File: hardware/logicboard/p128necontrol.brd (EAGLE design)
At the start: 95 x 72 mm, 57 parts, among them IC1 74LS158N, IC10 74LS595D, IC11 74LS595D, IC12 74LS595D, IC13 74LS595D, IC14 74LS595D, IC15 74LS595D, IC16 74LS595D, IC17 74LS595D, IC2 74LS595D, IC3 74LS595D, IC4 74LS595D, IC5 74LS595D, IC6 74LS595D, IC7 74LS595D, IC8 74LS595D, IC9 74LS595D, J2 DIN5

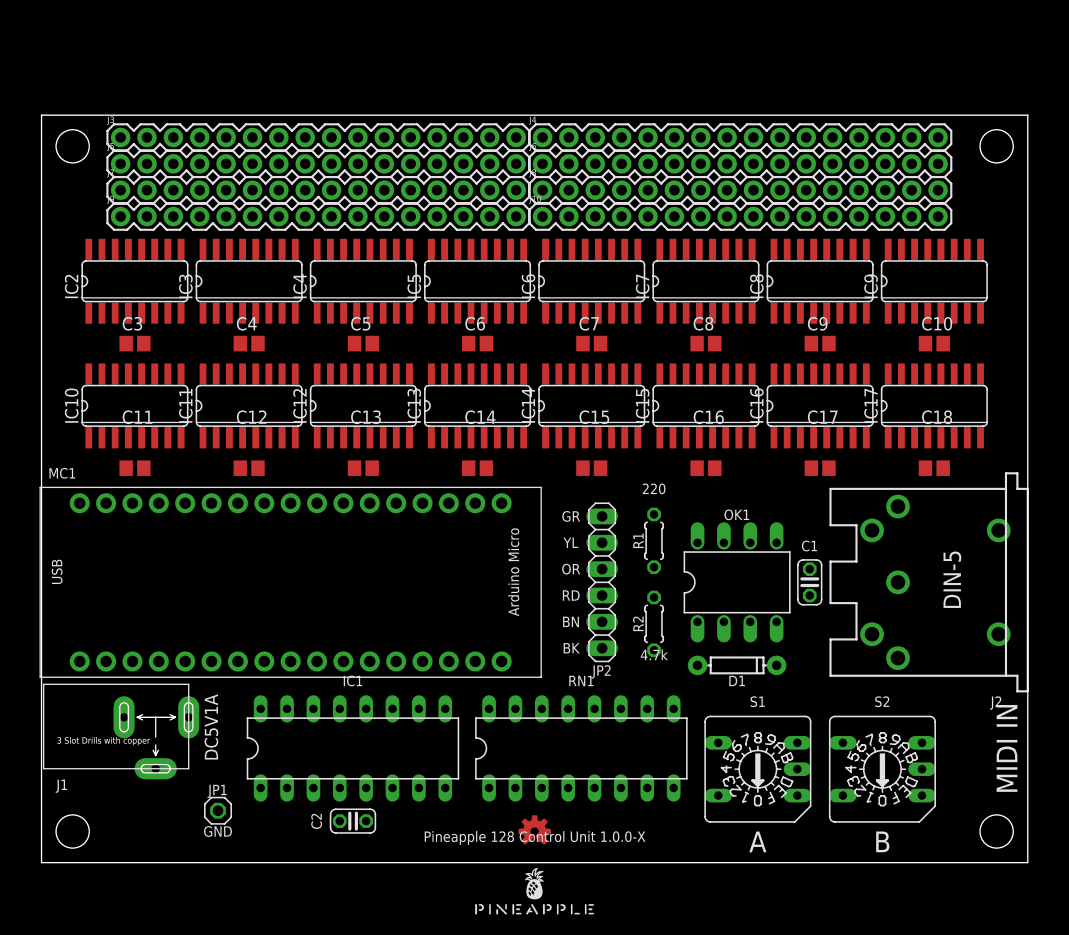
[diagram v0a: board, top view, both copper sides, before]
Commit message: Nocontrol 128-ch out.
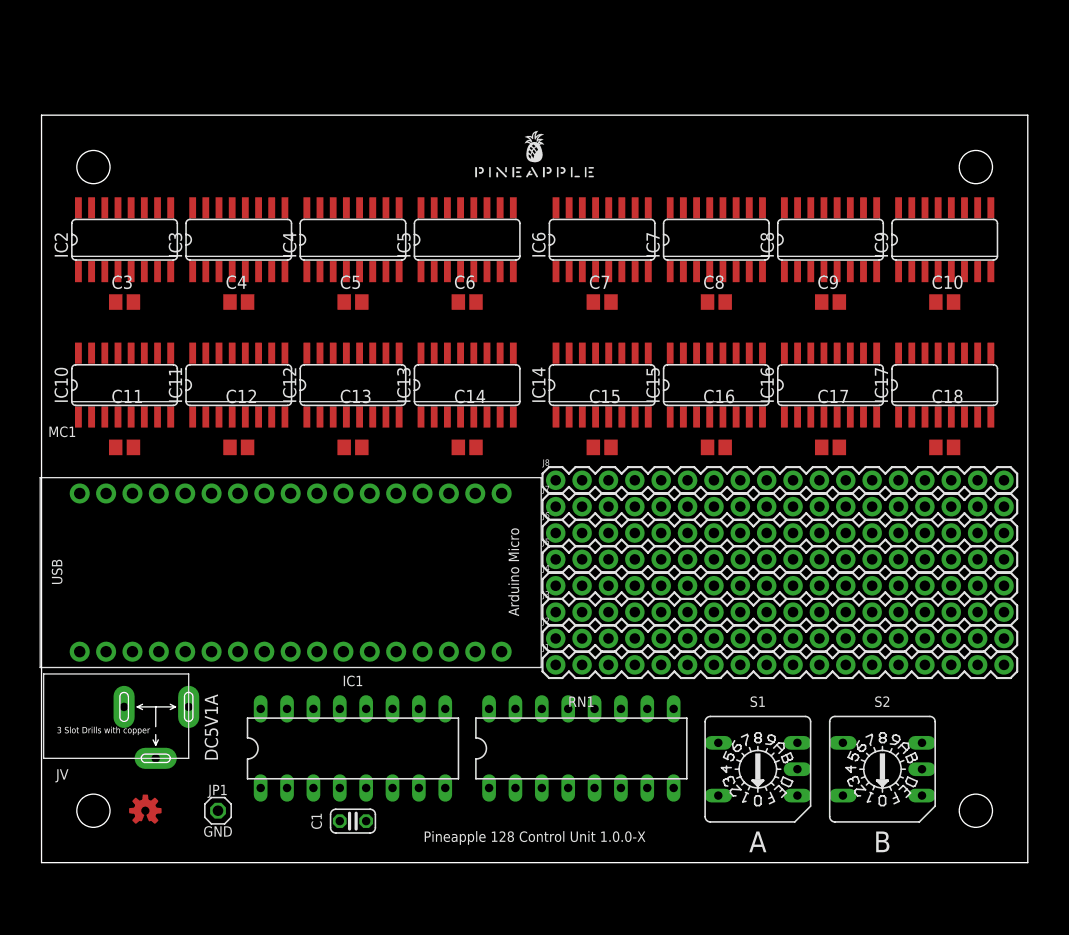
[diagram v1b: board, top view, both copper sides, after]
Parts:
- removed C2: (no value), resistor:C025-024X044
- removed D1: 200mA/100V/1V, SparkFun-DiscreteSemi:DIODE-1N4148
- removed J10, J9: (no value), SparkFun-Connectors:1X16
- removed JP2: (no value), pinhead:1X06
- removed OK1: 6N137, optocoupler:DIL08
- removed R1: 220, resistor:0204/5
- removed R2: 10k, resistor:0204/5
- added JV: (no value), Seeed-Connector:3P-L14.2*W11.0*H9.0MM
- J1: device Seeed-Connector:3P-L14.2*W11.0*H9.0MM -> SparkFun-Connectors:1X18
- J2: value DIN5 -> (none); device SparkFun-Connectors:DIN5-RA-PTH -> SparkFun-Connectors:1X18
- J3, J4, J5, J6, J7, J8: device SparkFun-Connectors:1X16 -> SparkFun-Connectors:1X18
- moved U$1 71.0 mm to (47.5, 66.0)
- moved J3 62.0 mm to (49.5, 24.1)
- moved J5 56.6 mm to (49.5, 29.2)
- moved J7 51.8 mm to (49.5, 34.3)
- moved C1 49.6 mm to (30.0, 4.00), turned to 180 degrees
- moved J2 45.8 mm to (49.5, 21.6), turned to 0 degrees
- moved J4 43.2 mm to (49.5, 26.7)
- moved J1 38.9 mm to (49.5, 19.1)
- moved LOGO1 37.6 mm to (10.0, 5.00)
- moved J6 35.6 mm to (49.5, 31.8)
- moved J8 28.0 mm to (49.5, 36.8)
- moved C10 4.12 mm to (87.0, 54.0)
- moved C3 4.12 mm to (8.00, 54.0)
- moved C4 4.12 mm to (19.0, 54.0)
- moved C5 4.12 mm to (30.0, 54.0)
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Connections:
- removed net MIRETN: D1.A, J2.5, OK1.3
- removed net MISEND: J2.4, R1.2
- removed net N$1: D1.C, OK1.2, R1.1
- net GND: now also J1.18, J1.9, J2.18, J2.9, J3.18, J3.9, J4.18, J4.9, J5.18, J5.9, J6.18, J6.9, J7.18, J7.9, J8.18, J8.9, JV.-1, JV.-2; no longer C2.2, J1.-1, J1.-2, JP2.1, JP2.2, OK1.5
- net N101: now also J1.1; no longer J3.1
- net N102: now also J1.2; no longer J3.2
- net N103: now also J1.3; no longer J3.3
- net N104: now also J1.4; no longer J3.4
- net N105: now also J1.5; no longer J3.5
- net N106: now also J1.6; no longer J3.6
- net N107: now also J1.7; no longer J3.7
- net N108: now also J1.8; no longer J3.8
- net N109: now also J1.10; no longer J3.9
- net N110: now also J1.11; no longer J3.10
- net N111: now also J1.12; no longer J3.11
- net N112: now also J1.13; no longer J3.12
- net N113: now also J1.14; no longer J3.13
- net N114: now also J1.15; no longer J3.14
- net N115: now also J1.16; no longer J3.15
- net N116: now also J1.17; no longer J3.16
- net N201: now also J2.1; no longer J4.1
- net N202: now also J2.2; no longer J4.2
- net N203: now also J2.3; no longer J4.3
- net N204: now also J2.4; no longer J4.4
- net N205: now also J2.5; no longer J4.5
- net N206: now also J2.6; no longer J4.6
- net N207: now also J2.7; no longer J4.7
- net N208: now also J2.8; no longer J4.8
- net N209: now also J2.10; no longer J4.9
- net N210: now also J2.11; no longer J4.10
- net N211: now also J2.12; no longer J4.11
- net N212: now also J2.13; no longer J4.12
- net N213: now also J2.14; no longer J4.13
- net N214: now also J2.15; no longer J4.14
- net N215: now also J2.16; no longer J4.15
- net N216: now also J2.17; no longer J4.16
- net N301: now also J3.1; no longer J5.1
- net N302: now also J3.2; no longer J5.2
- net N303: now also J3.3; no longer J5.3
- net N304: now also J3.4; no longer J5.4
- net N305: now also J3.5; no longer J5.5
- net N306: now also J3.6; no longer J5.6
- net N307: now also J3.7; no longer J5.7
- net N308: now also J3.8; no longer J5.8
- net N309: now also J3.10; no longer J5.9
- net N310: now also J3.11; no longer J5.10
- net N311: now also J3.12; no longer J5.11
- net N312: now also J3.13; no longer J5.12
- net N313: now also J3.14; no longer J5.13
- net N314: now also J3.15; no longer J5.14
- net N315: now also J3.16; no longer J5.15
- net N316: now also J3.17; no longer J5.16
- net N401: now also J4.1; no longer J6.1
- net N402: now also J4.2; no longer J6.2
- net N403: now also J4.3; no longer J6.3
- net N404: now also J4.4; no longer J6.4
- net N405: now also J4.5; no longer J6.5
- net N406: now also J4.6; no longer J6.6
- net N407: now also J4.7; no longer J6.7
- net N408: now also J4.8; no longer J6.8
- net N409: now also J4.10; no longer J6.9
- net N410: now also J4.11; no longer J6.10
- net N411: now also J4.12; no longer J6.11
- net N412: now also J4.13; no longer J6.12
- net N413: now also J4.14; no longer J6.13
- net N414: now also J4.15; no longer J6.14
- net N415: now also J4.16; no longer J6.15
- net N416: now also J4.17; no longer J6.16
- net N501: now also J5.1; no longer J7.1
- net N502: now also J5.2; no longer J7.2
- net N503: now also J5.3; no longer J7.3
- net N504: now also J5.4; no longer J7.4
- net N505: now also J5.5; no longer J7.5
- net N506: now also J5.6; no longer J7.6
- net N507: now also J5.7; no longer J7.7
- net N508: now also J5.8; no longer J7.8
- net N509: now also J5.10; no longer J7.9
- net N510: now also J5.11; no longer J7.10
- net N511: now also J5.12; no longer J7.11
- net N512: now also J5.13; no longer J7.12
- net N513: now also J5.14; no longer J7.13
- net N514: now also J5.15; no longer J7.14
- net N515: now also J5.16; no longer J7.15
- net N516: now also J5.17; no longer J7.16
- net N601: now also J6.1; no longer J8.1
- net N602: now also J6.2; no longer J8.2
- net N603: now also J6.3; no longer J8.3
- net N604: now also J6.4; no longer J8.4
- net N605: now also J6.5; no longer J8.5
- net N606: now also J6.6; no longer J8.6
- net N607: now also J6.7; no longer J8.7
- net N608: now also J6.8; no longer J8.8
- net N609: now also J6.10; no longer J8.9
- net N610: now also J6.11; no longer J8.10
- net N611: now also J6.12; no longer J8.11
- net N612: now also J6.13; no longer J8.12
- net N613: now also J6.14; no longer J8.13
- net N614: now also J6.15; no longer J8.14
- net N615: now also J6.16; no longer J8.15
- net N616: now also J6.17; no longer J8.16
- net N701: now also J7.1; no longer J9.1
- net N702: now also J7.2; no longer J9.2
- net N703: now also J7.3; no longer J9.3
- net N704: now also J7.4; no longer J9.4
- net N705: now also J7.5; no longer J9.5
- net N706: now also J7.6; no longer J9.6
- net N707: now also J7.7; no longer J9.7
- net N708: now also J7.8; no longer J9.8
- net N709: now also J7.10; no longer J9.9
- net N710: now also J7.11; no longer J9.10
- net N711: now also J7.12; no longer J9.11
- net N712: now also J7.13; no longer J9.12
- net N713: now also J7.14; no longer J9.13
- net N714: now also J7.15; no longer J9.14
- net N715: now also J7.16; no longer J9.15
- net N716: now also J7.17; no longer J9.16
- net N801: now also J8.1; no longer J10.1
- net N802: now also J8.2; no longer J10.2
- net N803: now also J8.3; no longer J10.3
- net N804: now also J8.4; no longer J10.4
- net N805: now also J8.5; no longer J10.5
- net N806: now also J8.6; no longer J10.6
- net N807: now also J8.7; no longer J10.7
- net N808: now also J8.8; no longer J10.8
- net N809: now also J8.10; no longer J10.9
- net N810: now also J8.11; no longer J10.10
- net N811: now also J8.12; no longer J10.11
- net N812: now also J8.13; no longer J10.12
- net N813: now also J8.14; no longer J10.13
- net N814: now also J8.15; no longer J10.14
- net N815: now also J8.16; no longer J10.15
- net N816: now also J8.17; no longer J10.16
- net RX: no longer JP2.4, OK1.6, R2.1
- net TX: no longer JP2.5
- net VCC: now also JV.+; no longer C2.1, J1.+, JP2.3, OK1.7, OK1.8, R2.2
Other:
- board text removed: "220"
- board text removed: "4.7k"
- board text removed: "BK"
- board text removed: "BN"
- board text removed: "GR"
- board text removed: "MIDI IN"
- board text removed: "OR"
- board text removed: "RD"
- board text removed: "YL"

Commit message: First working necontrol.
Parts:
- removed C10, C11, C12, C13, C14, C15, C16, C17, C18, C9: (no value), resistor:C2012
- removed IC10, IC11, IC12, IC13, IC14, IC15, IC16, IC17, IC9: 74LS595D, 74xx-us:SO16
- removed RN1: 10k, resistor-dil:DIL16
- removed S1, S2: (no value), switch-dil:A1353HEX
- added C2: (no value), resistor:C025-024X044
- added SV1, SV2, SV3: (no value), con-ml:ML14
- C3, C4, C5, C6, C7, C8: device resistor:C2012 -> resistor:C025-024X044
- IC1: value 74LS158N -> 74LS595N
- IC2, IC3, IC4, IC5, IC6, IC7, IC8: value 74LS595D -> 74LS595N; device 74xx-us:SO16 -> 74xx-us:DIL16
- J1, J2, J3, J4, J5, J6, J7, J8: device SparkFun-Connectors:1X18 -> SparkFun-Connectors:1X10
- moved C1 61.1 mm to (8.00, 61.0)
- moved IC1 43.9 mm to (8.00, 49.0), turned to 270 degrees
- moved J1 29.6 mm to (24.1, 3.81)
- moved J2 29.6 mm to (24.1, 6.35)
- moved J3 28.4 mm to (24.1, 11.4)
- moved J4 28.4 mm to (24.1, 14.0)
- moved J5 25.5 mm to (52.1, 3.81)
- moved J6 25.5 mm to (52.1, 6.35)
- moved C5 25.0 mm to (54.0, 61.0)
- moved C6 25.0 mm to (65.0, 61.0)
- moved C3 23.1 mm to (30.0, 61.0)
- moved C4 23.1 mm to (41.0, 61.0)
- moved C7 23.1 mm to (76.0, 61.0)
- moved C8 23.1 mm to (87.0, 61.0)
- moved J7 23.0 mm to (52.1, 11.4)
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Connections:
- removed net N$2: IC2.9, IC3.14
- removed net N$3: IC4.9, IC5.14
- removed net N$4: IC6.9, IC7.14
- removed net N$5: IC8.9, IC9.14
- removed net N$6: IC10.9, IC11.14
- removed net N$7: IC12.9, IC13.14
- removed net N$8: IC14.9, IC15.14
- removed net N$9: IC16.9, IC17.14
- removed net N109: IC3.15, J1.10
- removed net N110: IC3.1, J1.11
- removed net N111: IC3.2, J1.12
- removed net N112: IC3.3, J1.13
- removed net N113: IC3.4, J1.14
- removed net N114: IC3.5, J1.15
- removed net N115: IC3.6, J1.16
- removed net N116: IC3.7, J1.17
- removed net N209: IC5.15, J2.10
- removed net N210: IC5.1, J2.11
- removed net N211: IC5.2, J2.12
- removed net N212: IC5.3, J2.13
- removed net N213: IC5.4, J2.14
- removed net N214: IC5.5, J2.15
- removed net N215: IC5.6, J2.16
- removed net N216: IC5.7, J2.17
- removed net N309: IC7.15, J3.10
- removed net N310: IC7.1, J3.11
- removed net N311: IC7.2, J3.12
- removed net N312: IC7.3, J3.13
- removed net N313: IC7.4, J3.14
- removed net N314: IC7.5, J3.15
- removed net N315: IC7.6, J3.16
- removed net N316: IC7.7, J3.17
- removed net N409: IC9.15, J4.10
- removed net N410: IC9.1, J4.11
- removed net N411: IC9.2, J4.12
- removed net N412: IC9.3, J4.13
- removed net N413: IC9.4, J4.14
- removed net N414: IC9.5, J4.15
- removed net N415: IC9.6, J4.16
- removed net N416: IC9.7, J4.17
- removed net N509: IC11.15, J5.10
- removed net N510: IC11.1, J5.11
- removed net N511: IC11.2, J5.12
- removed net N512: IC11.3, J5.13
- removed net N513: IC11.4, J5.14
- removed net N514: IC11.5, J5.15
- removed net N515: IC11.6, J5.16
- removed net N516: IC11.7, J5.17
- removed net N609: IC13.15, J6.10
- removed net N610: IC13.1, J6.11
- removed net N611: IC13.2, J6.12
- removed net N612: IC13.3, J6.13
- removed net N613: IC13.4, J6.14
- removed net N614: IC13.5, J6.15
- removed net N615: IC13.6, J6.16
- removed net N616: IC13.7, J6.17
- removed net N709: IC15.15, J7.10
- removed net N710: IC15.1, J7.11
- removed net N711: IC15.2, J7.12
- removed net N712: IC15.3, J7.13
- removed net N713: IC15.4, J7.14
- removed net N714: IC15.5, J7.15
- removed net N715: IC15.6, J7.16
- removed net N716: IC15.7, J7.17
- removed net N809: IC17.15, J8.10
- removed net N810: IC17.1, J8.11
- removed net N811: IC17.2, J8.12
- removed net N812: IC17.3, J8.13
- removed net N813: IC17.4, J8.14
- removed net N814: IC17.5, J8.15
- removed net N815: IC17.6, J8.16
- removed net N816: IC17.7, J8.17
- removed net SWA1: IC1.2, RN1.1, S1.1
- removed net SWA2: IC1.5, RN1.3, S1.4
- removed net SWA4: IC1.11, RN1.5, S1.8
- removed net SWA8: IC1.14, RN1.7, S1.2
- removed net SWB1: IC1.3, RN1.2, S2.1
- removed net SWB2: IC1.6, RN1.4, S2.4
- removed net SWB4: IC1.10, RN1.6, S2.8
- removed net SWB8: IC1.13, RN1.8, S2.2
- new net SIN1: IC1.14, SV2.6
- new net SIN2: IC2.14, SV2.7
- new net SIN3: IC3.14, SV2.8
- new net SIN4: IC4.14, SV2.9
- new net SIN5: IC5.14, SV2.10
- new net SIN6: IC6.14, SV2.11
- new net SIN7: IC7.14, SV2.12
- new net SIN8: IC8.14, SV2.13
- new net XOUT1: IC1.9, SV3.6
- new net XOUT2: IC2.9, SV3.7
- new net XOUT3: IC3.9, SV3.8
- new net XOUT4: IC4.9, SV3.9
- new net XOUT5: IC5.9, SV3.10
- new net XOUT6: IC6.9, SV3.11
- new net XOUT7: IC7.9, SV3.12
- new net XOUT8: IC8.9, SV3.13
- net CLR: now also IC1.10, SV1.3, SV2.3, SV3.3; no longer IC10.10, IC11.10, IC12.10, IC13.10, IC14.10, IC15.10, IC16.10, IC17.10, IC9.10
- net GND: now also C2.2, IC1.13, J1.10, J2.10, J3.10, J4.10, J5.10, J6.10, J7.10, J8.10, SV1.14, SV1.2, SV2.14, SV2.2, SV3.14, SV3.2; no longer C10.2, C11.2, C12.2, C13.2, C14.2, C15.2, C16.2, C17.2, C18.2, C9.2, IC1.15, IC10.13, IC10.8, IC11.13, IC11.8, IC12.13, IC12.8, IC13.13, IC13.8, IC14.13, IC14.8, IC15.13, IC15.8, IC16.13, IC16.8, IC17.13, IC17.8, IC9.13, IC9.8, J1.18, J2.18, J3.18, J4.18, J5.18, J6.18, J7.18, J8.18, S1.C, S2.C
- net N101: now also IC1.15; no longer IC2.15
- net N102: now also IC1.1; no longer IC2.1
- net N103: now also IC1.2; no longer IC2.2
- net N104: now also IC1.3; no longer IC2.3
- net N105: now also IC1.4; no longer IC2.4
- net N106: now also IC1.5; no longer IC2.5
- net N107: now also IC1.6; no longer IC2.6
- net N108: now also IC1.7; no longer IC2.7
- net N201: now also IC2.15; no longer IC4.15
- net N202: now also IC2.1; no longer IC4.1
- net N203: now also IC2.2; no longer IC4.2
- net N204: now also IC2.3; no longer IC4.3
- net N205: now also IC2.4; no longer IC4.4
- net N206: now also IC2.5; no longer IC4.5
- net N207: now also IC2.6; no longer IC4.6
- net N208: now also IC2.7; no longer IC4.7
- net N301: now also IC3.15; no longer IC6.15
- net N302: now also IC3.1; no longer IC6.1
- net N303: now also IC3.2; no longer IC6.2
- net N304: now also IC3.3; no longer IC6.3
- net N305: now also IC3.4; no longer IC6.4
- net N306: now also IC3.5; no longer IC6.5
- net N307: now also IC3.6; no longer IC6.6
- net N308: now also IC3.7; no longer IC6.7
- net N401: now also IC4.15; no longer IC8.15
- net N402: now also IC4.1; no longer IC8.1
- net N403: now also IC4.2; no longer IC8.2
- net N404: now also IC4.3; no longer IC8.3
- net N405: now also IC4.4; no longer IC8.4
- net N406: now also IC4.5; no longer IC8.5
- net N407: now also IC4.6; no longer IC8.6
- net N408: now also IC4.7; no longer IC8.7
- net N501: now also IC5.15; no longer IC10.15
- net N502: now also IC5.1; no longer IC10.1
- net N503: now also IC5.2; no longer IC10.2
- net N504: now also IC5.3; no longer IC10.3
- net N505: now also IC5.4; no longer IC10.4
- net N506: now also IC5.5; no longer IC10.5
- net N507: now also IC5.6; no longer IC10.6
- net N508: now also IC5.7; no longer IC10.7
- net N601: now also IC6.15; no longer IC12.15
- net N602: now also IC6.1; no longer IC12.1
- net N603: now also IC6.2; no longer IC12.2
- net N604: now also IC6.3; no longer IC12.3
- net N605: now also IC6.4; no longer IC12.4
- net N606: now also IC6.5; no longer IC12.5
- net N607: now also IC6.6; no longer IC12.6
- net N608: now also IC6.7; no longer IC12.7
- net N701: now also IC7.15; no longer IC14.15
- net N702: now also IC7.1; no longer IC14.1
- net N703: now also IC7.2; no longer IC14.2
- net N704: now also IC7.3; no longer IC14.3
- net N705: now also IC7.4; no longer IC14.4
- net N706: now also IC7.5; no longer IC14.5
- net N707: now also IC7.6; no longer IC14.6
- net N708: now also IC7.7; no longer IC14.7
- net N801: now also IC8.15; no longer IC16.15
- net N802: now also IC8.1; no longer IC16.1
- net N803: now also IC8.2; no longer IC16.2
- net N804: now also IC8.3; no longer IC16.3
- net N805: now also IC8.4; no longer IC16.4
- net N806: now also IC8.5; no longer IC16.5
- net N807: now also IC8.6; no longer IC16.6
- net N808: now also IC8.7; no longer IC16.7
- net RCLK: now also IC1.12, SV1.5, SV2.5, SV3.5; no longer IC10.12, IC11.12, IC12.12, IC13.12, IC14.12, IC15.12, IC16.12, IC17.12, IC9.12
- net SCLK: now also IC1.11, SV1.4, SV2.4, SV3.4; no longer IC10.11, IC11.11, IC12.11, IC13.11, IC14.11, IC15.11, IC16.11, IC17.11, IC9.11
- net SOUT1: now also SV1.6; no longer IC2.14
- net SOUT2: now also SV1.7; no longer IC4.14
- net SOUT3: now also SV1.8; no longer IC6.14
- net SOUT4: now also SV1.9; no longer IC8.14
- net SOUT5: now also SV1.10; no longer IC10.14
- net SOUT6: now also SV1.11; no longer IC12.14
- net SOUT7: now also SV1.12; no longer IC14.14
- net SOUT8: now also SV1.13; no longer IC16.14
- net SW1: no longer IC1.4
- net SW2: no longer IC1.7
- net SW4: no longer IC1.9
- net SW8: no longer IC1.12
- net SWSEL: no longer IC1.1
- net VCC: now also C2.1, SV1.1, SV2.1, SV3.1; no longer C10.1, C11.1, C12.1, C13.1, C14.1, C15.1, C16.1, C17.1, C18.1, C9.1, IC10.16, IC11.16, IC12.16, IC13.16, IC14.16, IC15.16, IC16.16, IC17.16, IC9.16, RN1.10, RN1.11, RN1.12, RN1.13, RN1.14, RN1.15, RN1.16, RN1.9
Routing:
- net GND: track 0.00 -> 571.8 mm, vias 0 -> 4
- net CLR: track 0.00 -> 255.5 mm, vias 0 -> 12
- net SCLK: track 0.00 -> 252.4 mm, vias 0 -> 7
- net VCC: track 0.00 -> 240.5 mm, vias 0 -> 2
- net RCLK: track 0.00 -> 235.3 mm, vias 0 -> 9
- net XOUT1: track 0.00 -> 104.1 mm, vias 0 -> 4
- net N802: track 0.00 -> 103.3 mm
- net N201: track 0.00 -> 93.4 mm, vias 0 -> 3
- net N702: track 0.00 -> 85.6 mm, vias 0 -> 2
- net N803: track 0.00 -> 85.4 mm, vias 0 -> 2
- net N804: track 0.00 -> 81.4 mm
- net N202: track 0.00 -> 79.9 mm, vias 0 -> 2
- net N106: track 0.00 -> 77.6 mm
- net N108: track 0.00 -> 77.1 mm
- net N105: track 0.00 -> 77.0 mm
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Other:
- board text removed: "A"
- board text removed: "B"

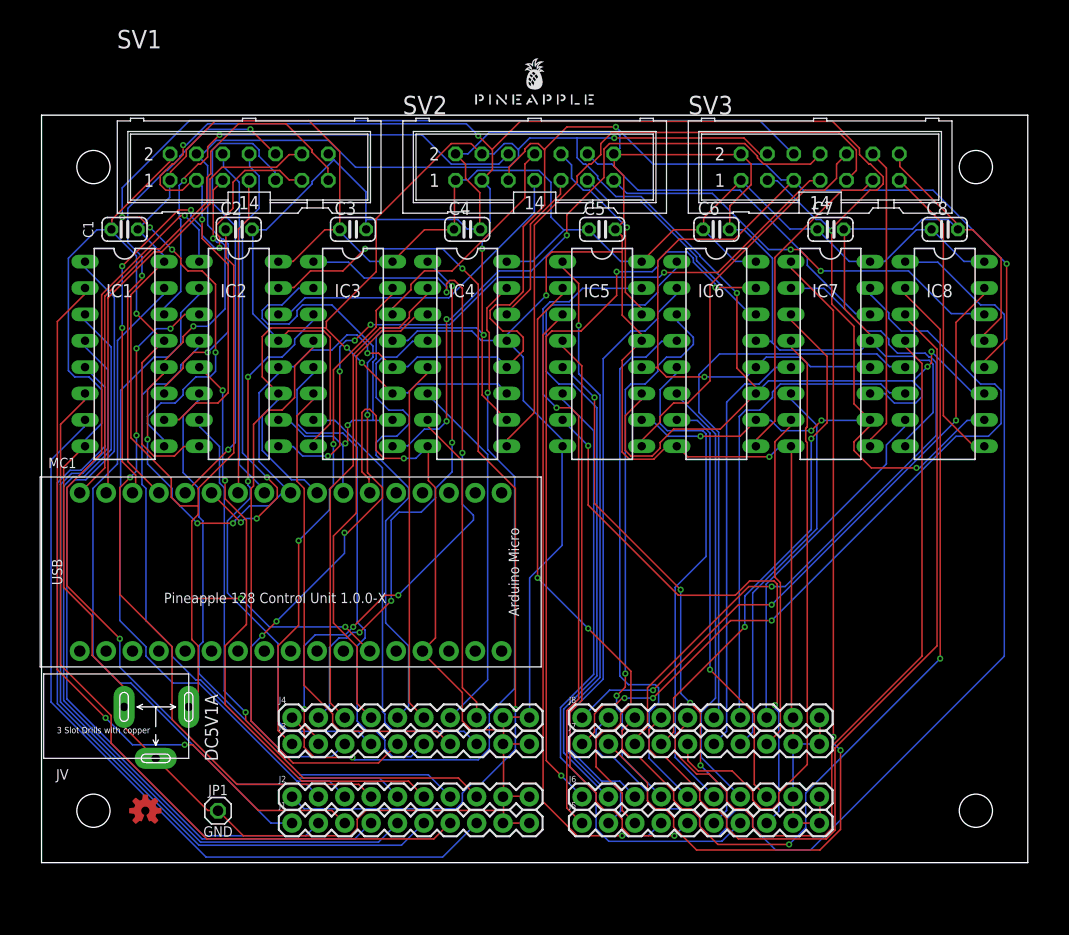
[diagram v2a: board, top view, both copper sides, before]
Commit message: Compiled Necontrol.
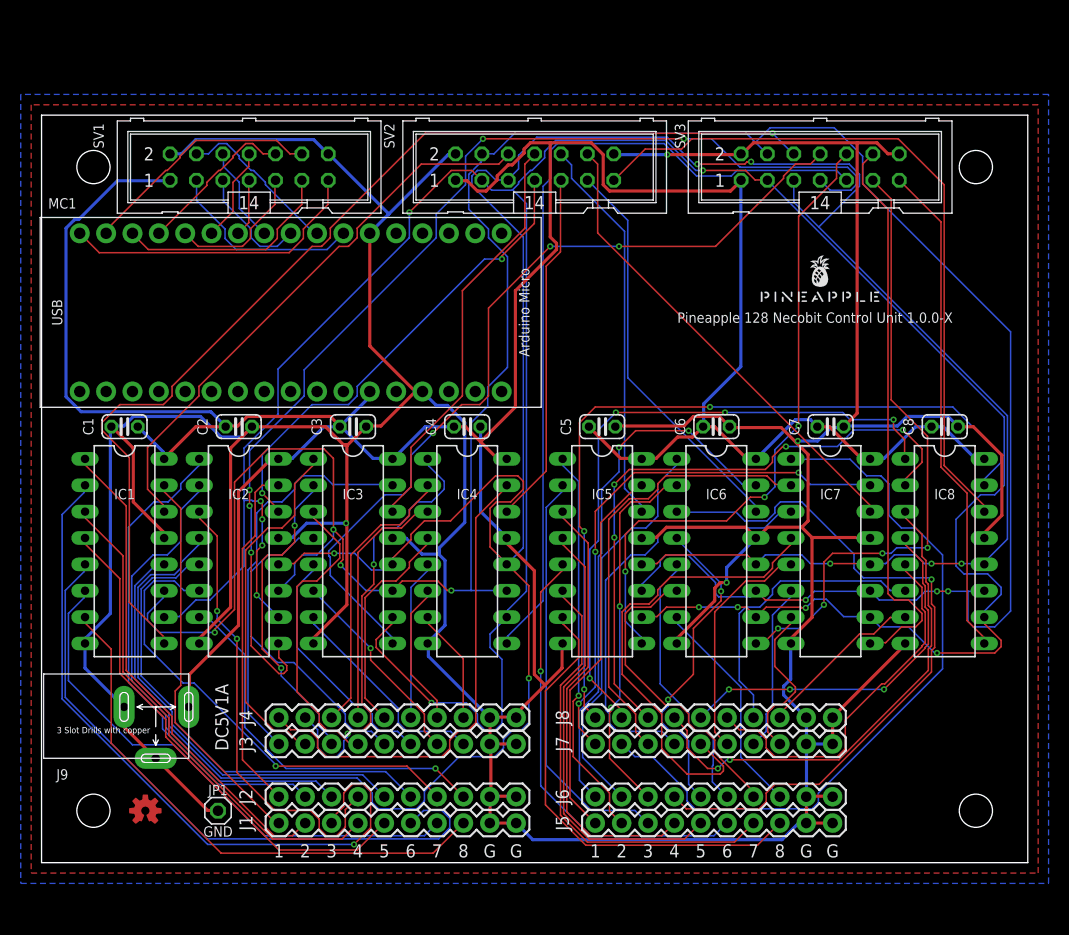
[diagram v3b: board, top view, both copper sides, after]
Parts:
- C1, C2, C3, C4, C5, C6, C7, C8: value (none) -> 0.01u
- SV1: value (none) -> OUT
- SV2: value (none) -> IN
- SV3: value (none) -> THRU
- moved U$1 33.4 mm to (75.0, 54.0)
- moved U$2 25.0 mm to (24.0, 53.0)
- moved C1 19.0 mm to (8.00, 42.0)
- moved C2 19.0 mm to (19.0, 42.0)
- moved C3 19.0 mm to (30.0, 42.0)
- moved C4 19.0 mm to (41.0, 42.0)
- moved C5 19.0 mm to (54.0, 42.0)
- moved C6 19.0 mm to (65.0, 42.0)
- moved C7 19.0 mm to (76.0, 42.0)
- moved C8 19.0 mm to (87.0, 42.0)
- moved IC1 19.0 mm to (8.00, 30.0)
- moved IC2 19.0 mm to (19.0, 30.0)
- moved IC3 19.0 mm to (30.0, 30.0)
- moved IC4 19.0 mm to (41.0, 30.0)
- moved IC5 19.0 mm to (54.0, 30.0)
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- renumbered JV to J9
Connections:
- removed net SW1: U$2.P$31
- removed net SW2: U$2.P$30
- removed net SW4: U$2.P$29
- removed net SW8: U$2.P$28
- removed net SWSEL: U$2.P$27
- new net CLROUT: SV1.3, U$2.P$11
- new net RCLKOUT: SV1.5, U$2.P$9
- new net SCLKOUT: SV1.4, U$2.P$10
- net CLR: no longer SV1.3, U$2.P$11
- net RCLK: no longer SV1.5, U$2.P$9
- net SCLK: no longer SV1.4, U$2.P$10
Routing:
- net N201: track 93.4 -> 33.8 mm, vias 3 -> 0
- net RCLK: track 235.3 -> 288.6 mm, vias 9 -> 7
- net GND: track 571.8 -> 527.9 mm
- net N303: track 73.5 -> 30.6 mm, vias 4 -> 2
- net N802: track 103.3 -> 63.0 mm, vias 0 -> 4
- net XOUT2: track 69.2 -> 108.2 mm
- net N805: track 74.9 -> 36.1 mm, vias 0 -> 3
- net N302: track 71.3 -> 34.4 mm, vias 5 -> 0
- net SOUT3: track 44.1 -> 9.14 mm, vias 3 -> 0
- net N804: track 81.4 -> 47.9 mm, vias 0 -> 2
- net SOUT5: track 48.2 -> 15.5 mm, vias 2 -> 0
- net N202: track 79.9 -> 47.4 mm, vias 2 -> 0
- net SOUT4: track 44.5 -> 13.7 mm, vias 1 -> 0
- net SOUT6: track 51.1 -> 21.6 mm, vias 4 -> 0
- net N602: track 68.0 -> 38.7 mm
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- added copper zone on layer 1, net GND
- added copper zone on layer 16, net GND
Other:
- board text added: "1"
- board text added: "2"
- board text added: "3"
- board text added: "4"
- board text added: "5"
- board text added: "6"
- board text added: "7"
- board text added: "8"
- board text added: "G"
- board text added: "IN"
- board text added: "OUT"
- board text added: "Pineapple 128 Necobit Control Unit 1.0.0-X"
- board text added: "THRU"
- board text removed: "Pineapple 128 Control Unit 1.0.0-X"
